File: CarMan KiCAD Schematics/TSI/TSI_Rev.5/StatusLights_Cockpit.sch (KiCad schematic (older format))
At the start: 20 parts, among them Q3 ZVP1320F, U1 RDE03110S12, U11 TLP293, U13 TLP293, U27 TLP293

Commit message: Aesthetics
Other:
- note added: "SIGNALS\n"
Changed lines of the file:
@@
 $Descr A4 11693 8268
 encoding utf-8
-Sheet 3 7
+Sheet 7 7
 Title ""
 Date ""
@@
 	6450 1300 6450 1150
 Connection ~ 5900 1300
-Text HLabel 1200 650  0    50   Input ~ 0
+Text HLabel 1250 800  0    50   Input ~ 0
 BP
-Text HLabel 1200 750  0    50   Input ~ 0
+Text HLabel 1250 900  0    50   Input ~ 0
 BP_RTN
-Text HLabel 1200 850  0    50   Input ~ 0
+Text HLabel 1250 1000 0    50   Input ~ 0
 IMD_Status
-Text HLabel 1200 950  0    50   Input ~ 0
+Text HLabel 1250 1100 0    50   Input ~ 0
 RTDS_CTRL
-Text HLabel 1200 1050 0    50   Input ~ 0
+Text HLabel 1250 1200 0    50   Input ~ 0
 D_LED_CTRL
-Text HLabel 1200 1150 0    50   Input ~ 0
+Text HLabel 1250 1300 0    50   Input ~ 0
 SPARE_LED_CTRL
-Text HLabel 1200 1750 0    50   Input ~ 0
+Text HLabel 1250 1600 0    50   Input ~ 0
 24V
-Text HLabel 1200 2050 0    50   Input ~ 0
-GLV_RTN
-Text HLabel 1200 1950 0    50   Input ~ 0
+Text HLabel 1250 1900 0    50   Input ~ 0
+GLV_RTN
+Text HLabel 1250 1800 0    50   Input ~ 0
 3.3V
-Text HLabel 1200 1850 0    50   Input ~ 0
+Text HLabel 1250 1700 0    50   Input ~ 0
 5V
 Wire Wire Line
-	1200 650  1350 650
-Wire Wire Line
-	1200 750  1350 750
-Wire Wire Line
-	1200 850  1350 850
-Wire Wire Line
-	1200 950  1350 950
-Wire Wire Line
-	1200 1050 1350 1050
-Wire Wire Line
-	1200 1150 1350 1150
-Wire Wire Line
-	1200 1750 1350 1750
-Wire Wire Line
-	1200 2050 1350 2050
-Wire Wire Line
-	1200 1950 1350 1950
-Wire Wire Line
-	1200 1850 1350 1850
-Text Label 1350 650  0    50   ~ 0
+	1250 800  1400 800
+Wire Wire Line
+	1250 900  1400 900
+Wire Wire Line
+	1250 1000 1400 1000
+Wire Wire Line
+	1250 1100 1400 1100
+Wire Wire Line
+	1250 1200 1400 1200
+Wire Wire Line
+	1250 1300 1400 1300
+Wire Wire Line
+	1250 1600 1400 1600
+Wire Wire Line
+	1250 1900 1400 1900
+Wire Wire Line
+	1250 1800 1400 1800
+Wire Wire Line
+	1250 1700 1400 1700
+Text Label 1400 800  0    50   ~ 0
 BP
-Text Label 1350 750  0    50   ~ 0
+Text Label 1400 900  0    50   ~ 0
 BP_RTN
-Text Label 1350 850  0    50   ~ 0
+Text Label 1400 1000 0    50   ~ 0
 IMD_Status
-Text Label 1350 950  0    50   ~ 0
+Text Label 1400 1100 0    50   ~ 0
 RTDS_CTRL
-Text Label 1350 1050 0    50   ~ 0
+Text Label 1400 1200 0    50   ~ 0
 D_LED_CTRL
-Text Label 1350 1150 0    50   ~ 0
+Text Label 1400 1300 0    50   ~ 0
 SPARE_LED_CTRL
-Text Label 1350 1750 0    50   ~ 0
+Text Label 1400 1600 0    50   ~ 0
 24V
-Text Label 1350 2050 0    50   ~ 0
-GLV_RTN
-Text Label 1350 1950 0    50   ~ 0
+Text Label 1400 1900 0    50   ~ 0
+GLV_RTN
+Text Label 1400 1800 0    50   ~ 0
 3.3V
-Text Label 1350 1850 0    50   ~ 0
+Text Label 1400 1700 0    50   ~ 0
 5V
 $Comp
@@
 Wire Notes Line
 	8350 5000 8200 5000
-Text HLabel 1200 2250 0    50   Input ~ 0
+Text HLabel 1250 2000 0    50   Input ~ 0
 TSAL
-Text HLabel 1200 2450 0    50   Input ~ 0
+Text HLabel 1250 2200 0    50   Input ~ 0
 TSAL_RTN
 Wire Wire Line
-	1200 2250 1350 2250
-Wire Wire Line
-	1200 2450 1350 2450
-Text Label 1350 2250 0    50   ~ 0
+	1250 2000 1400 2000
+Wire Wire Line
+	1250 2200 1400 2200
+Text Label 1400 2000 0    50   ~ 0
 TSAL
-Text Label 1350 2450 0    50   ~ 0
+Text Label 1400 2200 0    50   ~ 0
 TSAL_RTN
-Text HLabel 1200 2350 0    50   Input ~ 0
+Text HLabel 1250 2100 0    50   Input ~ 0
 TSAL_Cockpit
 Wire Wire Line
-	1200 2350 1350 2350
-Text Label 1350 2350 0    50   ~ 0
+	1250 2100 1400 2100
+Text Label 1400 2100 0    50   ~ 0
 TSAL_Cockpit
 Text Label 10200 2350 2    50   ~ 0
@@
 Wire Wire Line
 	10200 1450 10200 1650
-Text HLabel 1200 2650 0    50   Input ~ 0
+Text HLabel 1250 2400 0    50   Input ~ 0
 Drive_BTN_RTN
 Wire Wire Line
-	1200 2650 1350 2650
-Text Label 1350 2650 0    50   ~ 0
+	1250 2400 1400 2400
+Text Label 1400 2400 0    50   ~ 0
 Drive_BTN_RTN
-Text HLabel 1200 2550 0    50   Input ~ 0
+Text HLabel 1250 2300 0    50   Input ~ 0
 Drive_BTN
 Wire Wire Line
-	1200 2550 1350 2550
-Text Label 1350 2550 0    50   ~ 0
+	1250 2300 1400 2300
+Text Label 1400 2300 0    50   ~ 0
 Drive_BTN
 Wire Wire Line
@@
 Wire Wire Line
 	8050 6150 8050 5950
-Text HLabel 1200 1250 0    50   Input ~ 0
+Text HLabel 1250 1400 0    50   Input ~ 0
 RTDS
 Wire Wire Line
-	1200 1250 1350 1250
-Text Label 1350 1250 0    50   ~ 0
+	1250 1400 1400 1400
+Text Label 1400 1400 0    50   ~ 0
 RTDS
-Text Label 1350 1350 0    50   ~ 0
+Text Label 1400 1500 0    50   ~ 0
 RTDS_RTN
-Text HLabel 1200 1350 0    50   Input ~ 0
+Text HLabel 1250 1500 0    50   Input ~ 0
 RTDS_RTN
 Wire Wire Line
-	1200 1350 1350 1350
+	1250 1500 1400 1500
+Wire Notes Line
+	2100 500  500  500
+Wire Notes Line
+	500  2500 2100 2500
+Wire Notes Line
+	2100 500  2100 2500
+Wire Notes Line
+	500  500  500  2500
+Text Notes 1050 650  0    94   ~ 0
+SIGNALS\n
 $EndSCHEMATC

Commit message: Aesthetics, IMD Relay
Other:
- moved on the sheet: R15, R25, U11, U27
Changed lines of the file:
@@
 $Descr A4 11693 8268
 encoding utf-8
-Sheet 7 7
+Sheet 6 6
 Title ""
 Date ""
@@
 L TSI_Rev.5-rescue:TLP293-CarMan_KiCAD_Library-TSI_Rev.5-rescue U11
 U 1 1 5F9A966C
-P 4550 2350
-F 0 "U11" H 4550 2550 50  0000 C CNN
-F 1 "TLP293" H 4550 2150 50  0000 C CNN
-F 2 "Package_SO:SOIC-4_4.55x2.6mm_P1.27mm" H 4350 2150 50  0001 L CIN
-F 3 "" H 4550 2350 50  0001 L CNN
-	1    4550 2350
+P 4550 2100
+F 0 "U11" H 4550 2300 50  0000 C CNN
+F 1 "TLP293" H 4550 1900 50  0000 C CNN
+F 2 "Package_SO:SOIC-4_4.55x2.6mm_P1.27mm" H 4350 1900 50  0001 L CIN
+F 3 "" H 4550 2100 50  0001 L CNN
+	1    4550 2100
 	1    0    0    -1
 $EndComp
@@
 L TSI_Rev.5-rescue:TLP293-CarMan_KiCAD_Library-TSI_Rev.5-rescue U27
 U 1 1 5F9AA400
-P 4550 3150
-F 0 "U27" H 4550 3350 50  0000 C CNN
-F 1 "TLP293" H 4550 2950 50  0000 C CNN
-F 2 "Package_SO:SOIC-4_4.55x2.6mm_P1.27mm" H 4350 2950 50  0001 L CIN
-F 3 "" H 4550 3150 50  0001 L CNN
-	1    4550 3150
+P 4550 2900
+F 0 "U27" H 4550 3100 50  0000 C CNN
+F 1 "TLP293" H 4550 2700 50  0000 C CNN
+F 2 "Package_SO:SOIC-4_4.55x2.6mm_P1.27mm" H 4350 2700 50  0001 L CIN
+F 3 "" H 4550 2900 50  0001 L CNN
+	1    4550 2900
 	1    0    0    -1
 $EndComp
@@
 L Device:R R15
 U 1 1 5F9DEF51
-P 3900 2250
-F 0 "R15" V 3800 2250 50  0000 C CNN
-F 1 "300" V 3900 2250 50  0000 C CNN
-F 2 "" V 3830 2250 50  0001 C CNN
-F 3 "~" H 3900 2250 50  0001 C CNN
-	1    3900 2250
-	0    1    1    0
-$EndComp
-Wire Wire Line
-	3750 2250 3500 2250
-Text Label 5050 2250 0    50   ~ 0
+P 3900 2000
+F 0 "R15" V 3800 2000 50  0000 C CNN
+F 1 "300" V 3900 2000 50  0000 C CNN
+F 2 "" V 3830 2000 50  0001 C CNN
+F 3 "~" H 3900 2000 50  0001 C CNN
+	1    3900 2000
+	0    1    1    0
+$EndComp
+Wire Wire Line
+	3750 2000 3500 2000
+Text Label 5050 2000 0    50   ~ 0
 24V
-Text Label 5050 2450 0    50   ~ 0
+Text Label 5050 2200 0    50   ~ 0
 Drive_LED
-Text Label 4050 2450 2    50   ~ 0
-GLV_RTN
-Text Label 3500 2250 2    50   ~ 0
+Text Label 4050 2200 2    50   ~ 0
+GLV_RTN
+Text Label 3500 2000 2    50   ~ 0
 D_LED_CTRL
 Wire Wire Line
@@
 L Device:R R25
 U 1 1 5F9F8E38
-P 3900 3050
-F 0 "R25" V 3800 3050 50  0000 C CNN
-F 1 "300" V 3900 3050 50  0000 C CNN
-F 2 "" V 3830 3050 50  0001 C CNN
-F 3 "~" H 3900 3050 50  0001 C CNN
-	1    3900 3050
-	0    1    1    0
-$EndComp
-Wire Wire Line
-	3750 3050 3500 3050
-Text Label 4050 3250 2    50   ~ 0
-GLV_RTN
-Text Label 5050 3250 0    50   ~ 0
+P 3900 2800
+F 0 "R25" V 3800 2800 50  0000 C CNN
+F 1 "300" V 3900 2800 50  0000 C CNN
+F 2 "" V 3830 2800 50  0001 C CNN
+F 3 "~" H 3900 2800 50  0001 C CNN
+	1    3900 2800
+	0    1    1    0
+$EndComp
+Wire Wire Line
+	3750 2800 3500 2800
+Text Label 4050 3000 2    50   ~ 0
+GLV_RTN
+Text Label 5050 3000 0    50   ~ 0
 SPARE_LED
-Text Label 5050 3050 0    50   ~ 0
+Text Label 5050 2800 0    50   ~ 0
 24V
-Text Label 3500 3050 2    50   ~ 0
+Text Label 3500 2800 2    50   ~ 0
 SPARE_LED_CTRL
 $Comp
@@
 Text Notes 7200 1200 0    50   ~ 0
 0.2A Id *CHECK THIS FET, specifications\n are likely not correct.\n Placeholder transistor*
-Text Notes 4200 2800 0    50   ~ 0
+Text Notes 4200 2550 0    50   ~ 0
 Current Ratio 50%
 $Comp
@@
 Drive_BTN
 Wire Wire Line
-	5050 3250 4850 3250
-Wire Wire Line
-	5050 3050 4850 3050
-Wire Wire Line
-	4250 3050 4050 3050
-Wire Wire Line
-	4250 3250 4050 3250
-Wire Wire Line
-	5050 2250 4850 2250
-Wire Wire Line
-	5050 2450 4850 2450
-Wire Wire Line
-	4250 2450 4050 2450
-Wire Wire Line
-	4250 2250 4050 2250
+	5050 3000 4850 3000
+Wire Wire Line
+	5050 2800 4850 2800
+Wire Wire Line
+	4250 2800 4050 2800
+Wire Wire Line
+	4250 3000 4050 3000
+Wire Wire Line
+	5050 2000 4850 2000
+Wire Wire Line
+	5050 2200 4850 2200
+Wire Wire Line
+	4250 2200 4050 2200
+Wire Wire Line
+	4250 2000 4050 2000
 Wire Wire Line
 	4250 1300 4050 1300

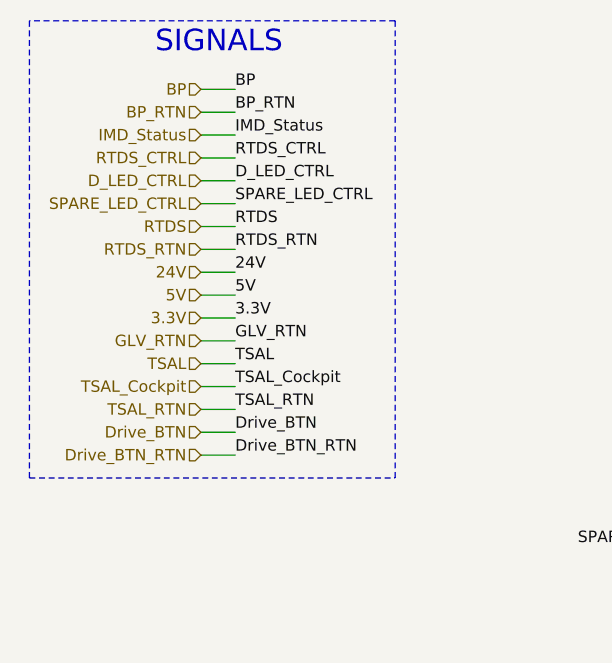
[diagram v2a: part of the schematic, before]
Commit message: Fixed some broken connections/errors on TSI
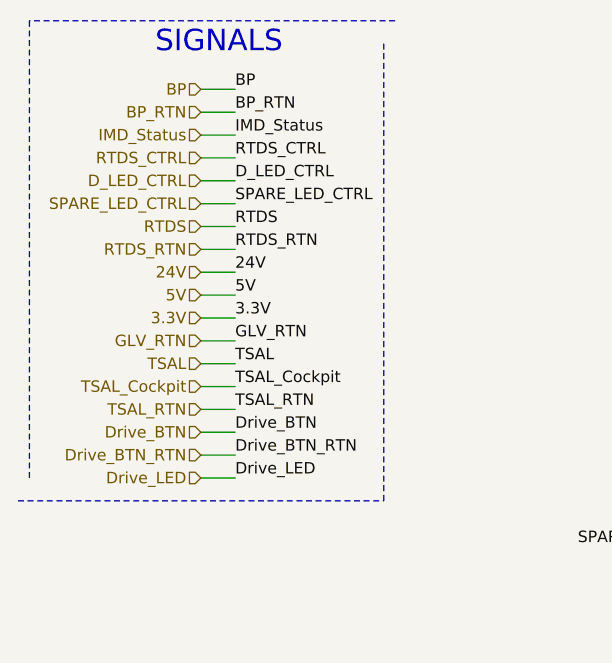
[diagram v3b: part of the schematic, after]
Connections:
- wire segments 84 -> 85
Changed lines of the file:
@@
 	2100 500  500  500
 Wire Notes Line
-	500  2500 2100 2500
+	450  2600 2050 2600
 Wire Notes Line
-	2100 500  2100 2500
+	2050 600  2050 2600
 Wire Notes Line
 	500  500  500  2500
 Text Notes 1050 650  0    94   ~ 0
 SIGNALS\n
+Text HLabel 1250 2500 0    50   Input ~ 0
+Drive_LED
+Wire Wire Line
+	1250 2500 1400 2500
+Text Label 1400 2500 0    50   ~ 0
+Drive_LED
 $EndSCHEMATC
